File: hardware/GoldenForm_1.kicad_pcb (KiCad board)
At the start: 4 copper layers, 60 x 40.5 mm, 27 parts, among them IC1 UVLO, J1 Conn_01x02_Pin, J2 1140084168, J3 Conn_01x04_Pin, J4 USB4105-GF-A, M3 MountingHole x 4, U2 BNO055, U3 Buck_Boost, U4 ESP32-S3-WROOM-1

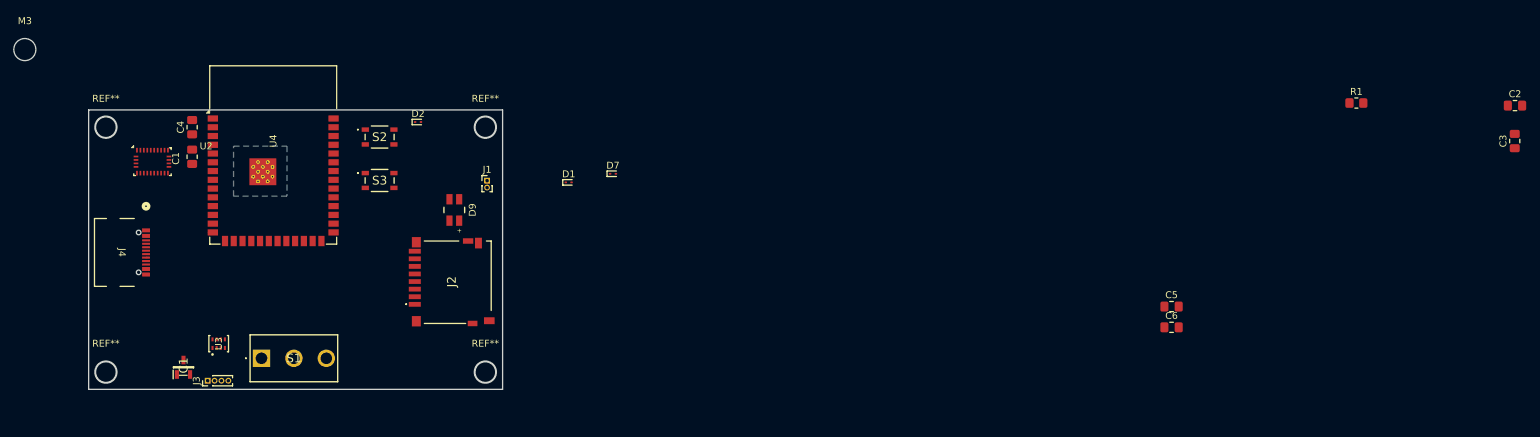
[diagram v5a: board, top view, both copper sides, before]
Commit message: placed the components on the PCB
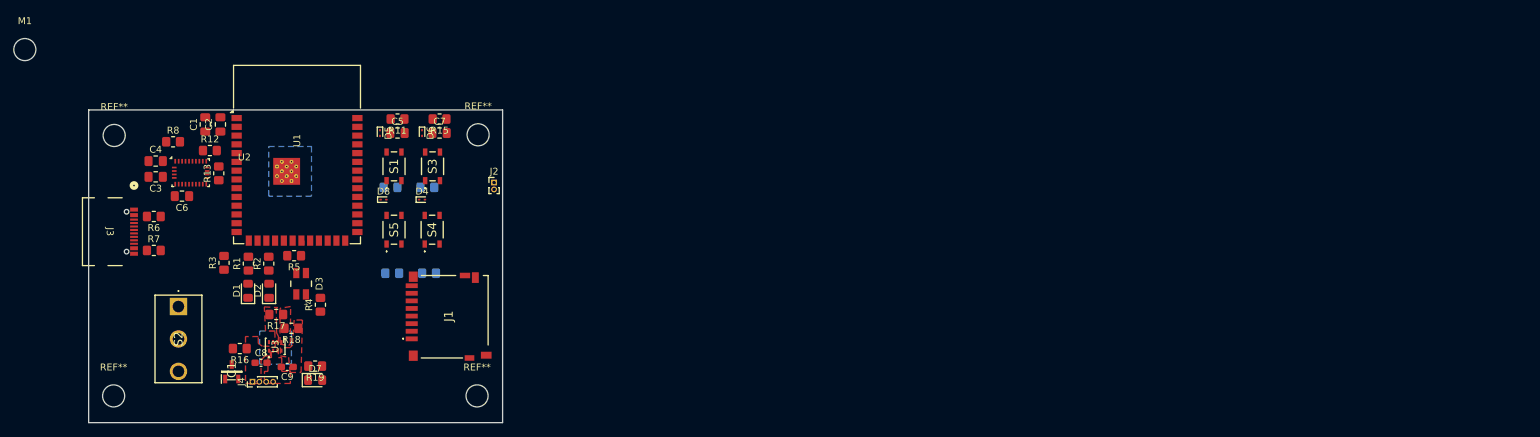
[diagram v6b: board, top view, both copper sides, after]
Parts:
- removed the C4 at (82.5, 53.0)
- added C5: 1uF, Capacitor_SMD:C_0805_2012Metric_Pad1.18x1.45mm_HandSolder, F.Cu at (112.3, 53.8)
- added C7: 1uF, Capacitor_SMD:C_0805_2012Metric_Pad1.18x1.45mm_HandSolder, F.Cu at (118.4, 53.8)
- added C8: 22uF, Capacitor_SMD:C_0603_1608Metric_Pad1.08x0.95mm_HandSolder, F.Cu at (92.5, 87.2)
- added C9: 47uF, Capacitor_SMD:C_0603_1608Metric_Pad1.08x0.95mm_HandSolder, F.Cu at (96.3, 87.8)
- added D2: START_STOP_LED, LED_SMD:LED_0805_2012Metric_Pad1.15x1.40mm_HandSolder, F.Cu at (93.7, 76.7)
- added D4: ESD3.3, Diode_SMD:D_SOD-923, F.Cu at (115.8, 63.5)
- added D7: POWER_LED, LED_SMD:LED_0805_2012Metric_Pad1.15x1.40mm_HandSolder, F.Cu at (100.3, 89.7)
- added D8: ESD3.3, Diode_SMD:D_SOD-923, F.Cu at (110.2, 63.5)
- added R1: 240, Resistor_SMD:R_0805_2012Metric_Pad1.20x1.40mm_HandSolder, F.Cu at (90.7, 72.8)
- added R10: 10k, Resistor_SMD:R_0805_2012Metric_Pad1.20x1.40mm_HandSolder, B.Cu at (116.6, 61.7)
- added R11: 10k, Resistor_SMD:R_0805_2012Metric_Pad1.20x1.40mm_HandSolder, F.Cu at (112.3, 51.8)
- added R12: 4.7k, Resistor_SMD:R_0805_2012Metric_Pad1.20x1.40mm_HandSolder, F.Cu at (85.1, 56.4)
- added R13: 4.7k, Resistor_SMD:R_0805_2012Metric_Pad1.20x1.40mm_HandSolder, F.Cu at (86.4, 59.7)
- added R14: 10k, Resistor_SMD:R_0805_2012Metric_Pad1.20x1.40mm_HandSolder, B.Cu at (111.3, 61.7)
- added R15: 10k, Resistor_SMD:R_0805_2012Metric_Pad1.20x1.40mm_HandSolder, F.Cu at (118.4, 51.8)
- added R17: 91k, Resistor_SMD:R_0805_2012Metric_Pad1.20x1.40mm_HandSolder, F.Cu at (94.7, 80.2)
- added R18: 511k, Resistor_SMD:R_0805_2012Metric_Pad1.20x1.40mm_HandSolder, F.Cu at (96.9, 82.2)
- added R19: 240, Resistor_SMD:R_0805_2012Metric_Pad1.20x1.40mm_HandSolder, F.Cu at (100.3, 87.6)
- added R2: 240, Resistor_SMD:R_0805_2012Metric_Pad1.20x1.40mm_HandSolder, F.Cu at (93.6, 72.8)
- added R21: 10k, Resistor_SMD:R_0805_2012Metric_Pad1.20x1.40mm_HandSolder, B.Cu at (116.8, 74.2)
- added R3: 1k, Resistor_SMD:R_0805_2012Metric_Pad1.20x1.40mm_HandSolder, F.Cu at (87.1, 72.7)
- added R4: 240, Resistor_SMD:R_0805_2012Metric_Pad1.20x1.40mm_HandSolder, F.Cu at (101.1, 78.7)
- added R5: 10k, Resistor_SMD:R_0805_2012Metric_Pad1.20x1.40mm_HandSolder, F.Cu at (97.3, 71.6)
- added R6: 5.1k, Resistor_SMD:R_0805_2012Metric_Pad1.20x1.40mm_HandSolder, F.Cu at (76.9, 65.9)
- added R7: 5.1k, Resistor_SMD:R_0805_2012Metric_Pad1.20x1.40mm_HandSolder, F.Cu at (76.9, 70.9)
- added R8: 10K, Resistor_SMD:R_0805_2012Metric_Pad1.20x1.40mm_HandSolder, F.Cu at (79.7, 55.1)
- added R9: 10k, Resistor_SMD:R_0805_2012Metric_Pad1.20x1.40mm_HandSolder, B.Cu at (111.5, 74.2)
- added S4: PTS810SJM250SMTR_LFS, MyFootprints:PTS810SJM250SMTRLFS, F.Cu at (117.3, 67.9)
- added S5: PTS810SJM250SMTR_LFS, MyFootprints:PTS810SJM250SMTRLFS, F.Cu at (111.8, 67.9)
- C1: value 20uF -> 22uF
- C2: value 10uF -> 0.1uF
- D1: value ESD3.3 -> SYNC_LED; footprint Diode_SMD:D_SOD-923 -> LED_SMD:LED_0805_2012Metric_Pad1.15x1.40mm_HandSolder
- D3: renamed from D9; value WL-SFTW_3528_PLCC4 -> Error_Leds
- moved C3 197.1 mm to (77.2, 60.2), turned to 180 degrees
- moved C2 187.7 mm to (86.6, 52.6), turned to 90 degrees
- moved R16 165.7 mm to (89.4, 85.1), turned to 180 degrees
- moved C4 149.2 mm to (77.2, 57.9)
- moved C6 144.3 mm to (81.0, 63.0), turned to 180 degrees
- moved D1 49.1 mm to (90.6, 76.7), turned to 90 degrees
- moved D5 34.3 mm to (109.7, 53.8), turned to -90 degrees
- moved D3 24.6 mm to (98.3, 75.7)
- moved S2 14.2 mm to (80.5, 79.0), turned to -90 degrees
- moved U3 8.20 mm to (94.5, 84.8)
- moved S3 7.94 mm to (117.3, 58.7), turned to 90 degrees
- moved IC1 7.02 mm to (88.2, 88.5)
- moved J4 6.49 mm to (91.2, 89.9)
- moved U2 5.77 mm to (82.3, 59.6)
- moved C1 5.06 mm to (84.4, 52.6)
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- renumbered C6 to C4, C5 to C6, D7 to D5, D2 to D6, J2 to J1, J1 to J2, J4 to J3, J3 to J4, M3 to M1, R1 to R16, S2 to S1, S1 to S2, U4 to U1
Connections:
- C1 pad 1: GND -> V_DD
- C1 pad 2: V_DD -> GND
- C2 pad 1: V_Bat -> V_DD
- D1 pad 2: BOOT_PIN -> Net-(D1-A)
- D3 pad 2: SYNC_LED -> ERROR_LED3
- D3 pad 3: ERROR_LED -> ERROR_LED2
- D3 pad 4: LOG_LED -> ERROR_LED1
- J3 pad B4-A9: Net-(J4-VBUS-PadB4-A9) -> V_BUS
- S1 pad 1: unconnected-(S2-NO_1-Pad1) -> Net-(S1-NO_1)
- S1 pad 4: unconnected-(S2-COM_2-Pad4) -> GND
- S2 pad 1: unconnected-(S1-NC-Pad1) -> GND
- S3 pad 1: unconnected-(S3-NO_1-Pad1) -> Net-(S3-NO_1)
- S3 pad 4: unconnected-(S3-COM_2-Pad4) -> GND
- U1 pad 12: LOG_LED -> ERROR_LED3
- U1 pad 16: unconnected-(U4-IO46-Pad16) -> SYNC_BUTTON
- U1 pad 18: unconnected-(U4-IO10-Pad18) -> START_STOP_LED
- U1 pad 26: unconnected-(U4-IO45-Pad26) -> ST_BUTTON
- U1 pad 38: LOG_LED -> ERROR_LED2
- U1 pad 39: ERROR_LED -> ERROR_LED1
- U3 pad 5: Net-(U3-FB) -> FB
- U3 pad 7: V_DD -> MODE
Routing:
- net D+: track 1.06 -> 0.00 mm
- net unconnected-(U1-IO13-Pad21): track 0.00 -> 0.53 mm
- net SCK: track 0.53 -> 0.00 mm
- added copper zone on F.Cu, net FB
- added copper zone on F.Cu, net GND
- added copper zone on F.Cu, net V_Bat
- added copper zone on F.Cu, net V_DD
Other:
- board size 60 x 40.5 mm -> 60 x 45.3 mm

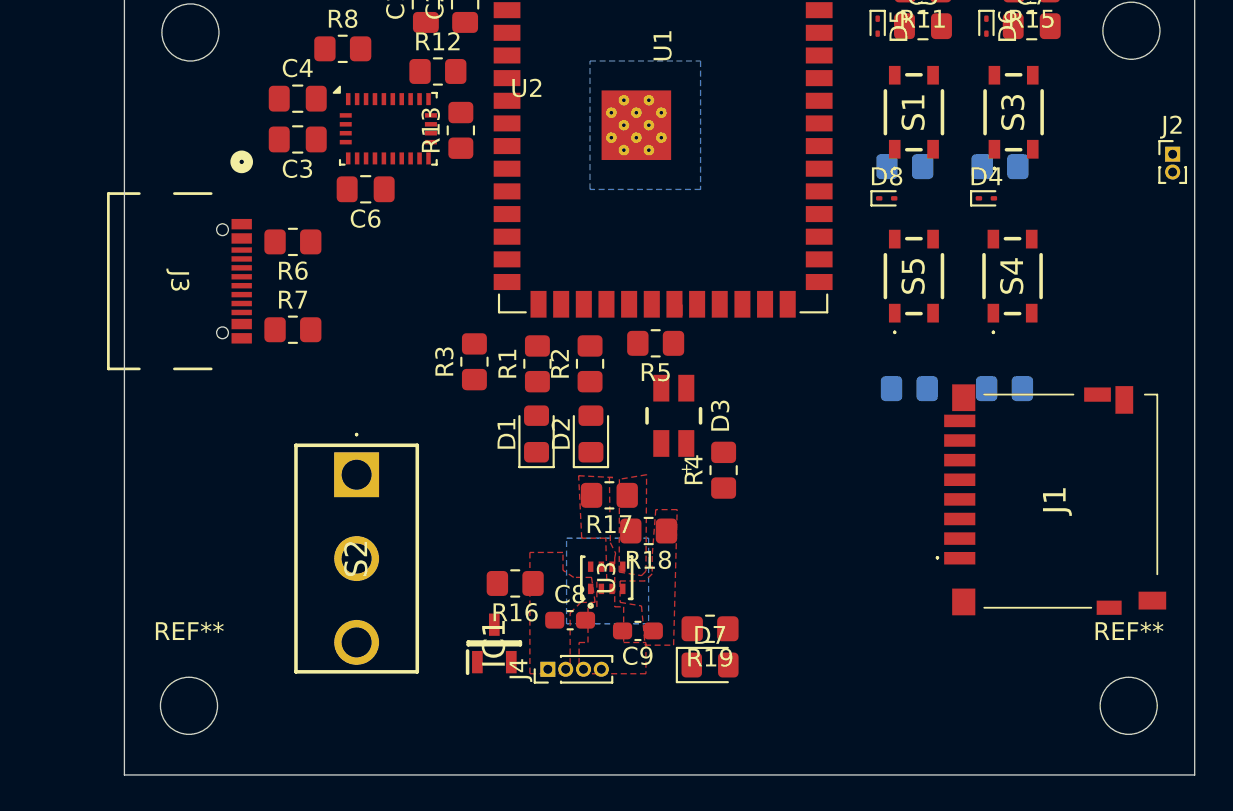
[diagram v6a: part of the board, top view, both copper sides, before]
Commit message: added transistor and haptic onto board
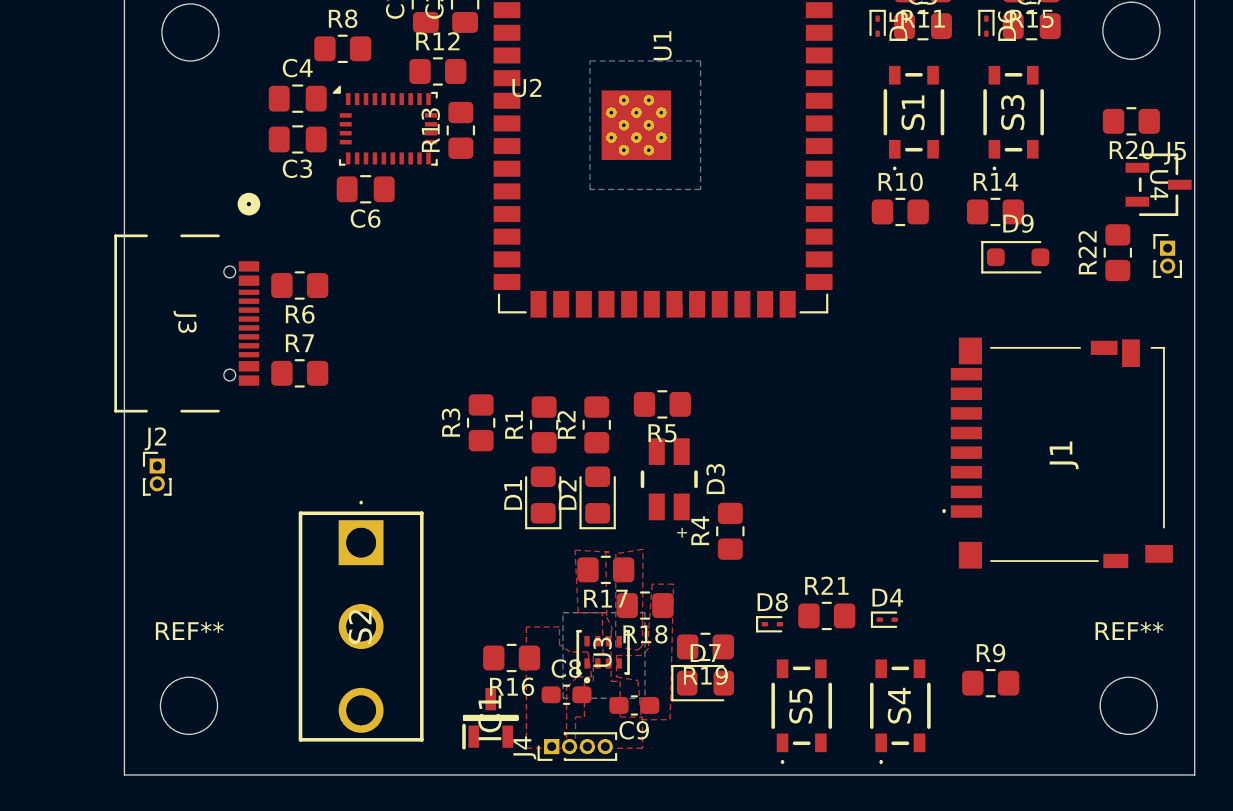
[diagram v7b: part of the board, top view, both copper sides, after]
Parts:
- added D9: D_Schottky, Diode_SMD:D_SOD-323_HandSoldering, F.Cu at (117.6, 66.8)
- added J5: Conn_01x02_Pin, Connector_PinHeader_1.00mm:PinHeader_1x02_P1.00mm_Vertical, F.Cu at (126.0, 66.3)
- added R20: 100, Resistor_SMD:R_0805_2012Metric_Pad1.20x1.40mm_HandSolder, F.Cu at (124.0, 59.2)
- added R22: 100k, Resistor_SMD:R_0805_2012Metric_Pad1.20x1.40mm_HandSolder, F.Cu at (123.2, 66.5)
- added U4: AO3400A, MyFootprints:SOT-23-3L_AOS, F.Cu at (125.5, 62.7)
- R10, R14, R21, R9: moved to F.Cu
- moved J2 59.5 mm to (69.3, 78.5)
- moved S5 24.9 mm to (105.5, 91.9)
- moved S4 24.9 mm to (111.0, 91.9)
- moved D8 24.7 mm to (103.8, 87.4)
- moved D4 24.3 mm to (110.3, 87.1)
- moved R9 17.1 mm to (116.1, 90.7), turned to 0 degrees
- moved R21 16.2 mm to (106.9, 86.9), turned to 0 degrees
- moved R10 6.14 mm to (111.0, 64.3), turned to 0 degrees
- moved R14 5.68 mm to (116.3, 64.3), turned to 0 degrees
- moved J4 4.34 mm to (91.5, 94.2)
- moved C8 4.18 mm to (92.3, 91.3)
- moved C9 4.18 mm to (96.1, 91.9)
- moved IC1 4.18 mm to (88.0, 92.6)
- moved R16 4.18 mm to (89.2, 89.3)
- moved R17 4.18 mm to (94.5, 84.3)
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
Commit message: started routing. added classes and stuff
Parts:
- C3: value C -> 100nF
- moved R5 20.8 mm to (117.6, 69.0), turned to 0 degrees
- moved R4 9.66 mm to (97.0, 73.6), turned to -90 degrees
- moved D1 2.60 mm to (91.0, 77.5)
- moved D2 2.60 mm to (94.0, 77.5)
- moved R1 2.60 mm to (91.0, 73.6)
- moved R2 2.60 mm to (94.0, 73.6)
- moved D3 1.08 mm to (97.8, 78.2), turned to 90 degrees
- moved R7 0.72 mm to (77.2, 72.6)
- moved R13 0.64 mm to (87.0, 59.7)
- moved U1 0.40 mm to (98.1, 56.9)
- moved C3 0.25 mm to (77.0, 60.2)
- moved C4 0.22 mm to (77.0, 57.9)
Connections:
- U1 pad 38: ERROR_LED2 -> ERROR_LED1
- U1 pad 39: ERROR_LED1 -> ERROR_LED2
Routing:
- net ERROR_LED2: track 0.00 -> 33.5 mm, vias 0 -> 2
- net ERROR_LED1: track 0.00 -> 32.0 mm, vias 0 -> 2
- net ERROR_LED3: track 0.00 -> 27.1 mm, vias 0 -> 2
- net CS: track 0.45 -> 19.8 mm
- net D-: track 0.00 -> 18.5 mm
- net D+: track 0.00 -> 18.5 mm
- net MOSI: track 0.00 -> 18.3 mm
- net SCK: track 0.00 -> 16.1 mm
- net UVLO_EN: track 0.00 -> 15.6 mm
- net MISO: track 0.00 -> 13.9 mm
- net BUCK_EN: track 0.00 -> 13.4 mm
- net GND: track 0.00 -> 13.4 mm, vias 0 -> 30
- net V_Bat: track 0.00 -> 9.16 mm
- net INT: track 0.00 -> 7.35 mm, vias 0 -> 2
- net SDA: track 0.00 -> 6.46 mm
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- removed copper zone on F.Cu, net FB
